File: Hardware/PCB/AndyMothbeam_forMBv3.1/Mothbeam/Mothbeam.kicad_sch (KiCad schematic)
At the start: 27 parts, among them CN1 X6511FRS-04-C85D30, SW2 SW_DIP_x04, U1 BCR421U, U2 BCR421U, U3 BCR421U, U4 M3535N1UVS8U12- 405NM, U5 M3535N1UVS8U06-385NM

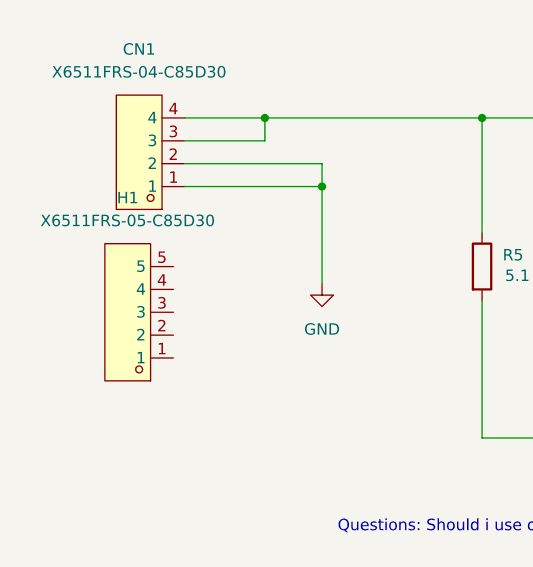
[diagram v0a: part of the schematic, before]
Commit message: no DRC errors on Mothbeam!
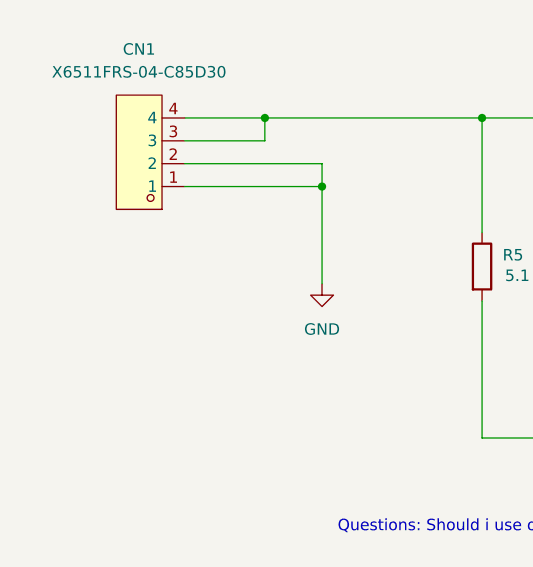
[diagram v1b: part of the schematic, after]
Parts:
- removed H1: X6511FRS-05-C85D30, easyeda2kicad:HDR-SMD_5P-P2.54-H-F_X6511FRS-19-C85D30, symbol easyeda2kicad:X6511FRS-05-C85D30
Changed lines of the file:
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@@
-	)
-	(symbol
-		(lib_id "easyeda2kicad:X6511FRS-05-C85D30")
-		(at 17.78 63.5 180)
-		(unit 1)
-		(exclude_from_sim no)
-		(in_bom yes)
-		(on_board yes)
-		(dnp no)
-		(fields_autoplaced yes)
-		(property "Reference" "H1"
-			(at 17.78 50.8 0)
-			(effects
-				(font
-					(size 1.27 1.27)
-				)
-			)
-		)
-		(property "Value" "X6511FRS-05-C85D30"
-			(at 17.78 53.34 0)
-			(effects
-				(font
-					(size 1.27 1.27)
-				)
-			)
-		)
-		(property "Footprint" "easyeda2kicad:HDR-SMD_5P-P2.54-H-F_X6511FRS-19-C85D30"
-			(at 17.78 50.8 0)
-			(effects
-				(font
-					(size 1.27 1.27)
-				)
-				(hide yes)
-			)
-		)
-		(property "Datasheet" ""
-			(at 17.78 63.5 0)
-			(effects
-				(font
-					(size 1.27 1.27)
-				)
-				(hide yes)
-			)
-		)
-		(property "Description" ""
-			(at 17.78 63.5 0)
-			(effects
-				(font
-					(size 1.27 1.27)
-				)
-				(hide yes)
-			)
-		)
-		(property "LCSC Part" "C5142238"
-			(at 17.78 48.26 0)
-			(effects
-				(font
-					(size 1.27 1.27)
-				)
-				(hide yes)
-			)
-		)
-		(pin "4"
-		)
-		(pin "1"
-		)
-		(pin "5"
-		)
-		(pin "2"
-		)
-		(pin "3"
-		)
-		(instances
-			(project ""
-				(path "/a270892a-30ca-43aa-91d1-ed114756b159"
-					(reference "H1")
-					(unit 1)
-				)
-			)
-		)
 	)
 	(symbol

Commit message: widen tiny bit track
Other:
- company: LabLab GmbH -> LabLab GmbH - modified by DINALAB
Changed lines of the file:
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@@
 		(date "2024-10-20")
 		(rev "A")
-		(company "LabLab GmbH")
+		(company "LabLab GmbH - modified by DINALAB")
 	)
 	(rectangle

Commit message: all LCSC parts except resistors!
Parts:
- D1: footprint easyeda2kicad:LED-SMD_3P-L3.5-W3.5_M3535O1IRS13G06 -> easyeda2kicad:LED-SMD_3P-L3.5-W3.5-R-RD-C; symbol Device:LED_Pad -> easyeda2kicad:M3535N1UVS8U12-365NM; LCSC Part (none) -> C2833504
- D2: symbol Device:LED_Pad -> easyeda2kicad:M3535N1UVS8U12-395NM; LCSC Part (none) -> C2833576
- D3: symbol Device:LED_Pad -> easyeda2kicad:M3535N1UVS8U12-405NM; LCSC Part (none) -> C2833578
- SW2: footprint Button_Switch_SMD:SW_DIP_SPSTx04_Slide_KingTek_DSHP04TS_W7.62mm_P1.27mm -> easyeda2kicad:SW-SMD_8P-L6.7-W5.4-P1.27-LS8.5; symbol Switch:SW_DIP_x04 -> easyeda2kicad:DSHP04TS-S; LCSC Part (none) -> C319050; PN 416131160804 -> (none)
- U1, U2, U3: footprint Package_TO_SOT_SMD:SC-74-6_1.55x2.9mm_P0.95mm -> easyeda2kicad:SOT-23-6_L2.9-W1.6-P0.95-LS2.8-BL; symbol LabLab:BCR421U -> easyeda2kicad:BCR421UW6-7; LCSC Part (none) -> C194382
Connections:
- net LED+: now also D1.1 (+); no longer D1.2 (A)
- net LED-: now also D3.2 (-), R2.1, R3.1, U1.6 (REXT); no longer D3.1 (K)
- new net: D1.2 (-), D2.1 (A), TP3.1
- new net: D2.2 (K), D3.1 (+), TP1.1
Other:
- moved on the sheet: R1, R9
